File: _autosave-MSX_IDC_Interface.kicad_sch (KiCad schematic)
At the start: 27 parts, among them J1 DE1 GPIO, J2 Conn_01x03_Male, J3 Conn_01x03_Male, J4 Conn_01x03_Male, J5 Conn_01x03_Male, J6 Conn_01x03_Male, J7 Conn_01x03_Male, Q1 2N2222, Q2 2N2222, U1 74LVC245A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

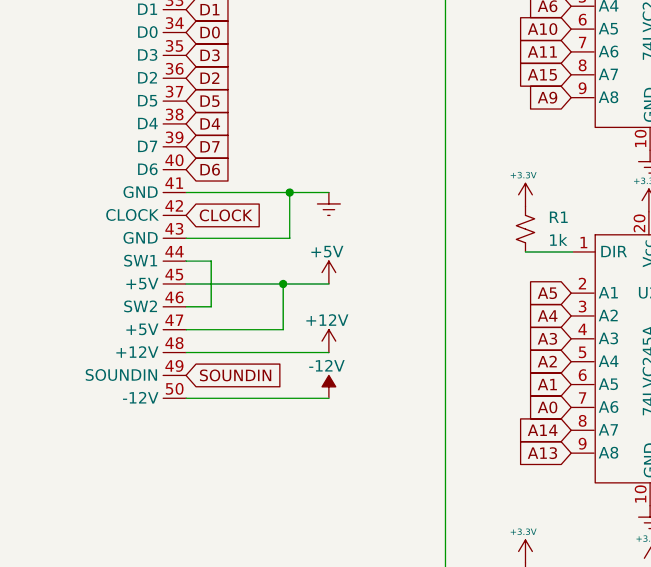
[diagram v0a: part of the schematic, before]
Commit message: Finished routing. Rules chekc not done yet
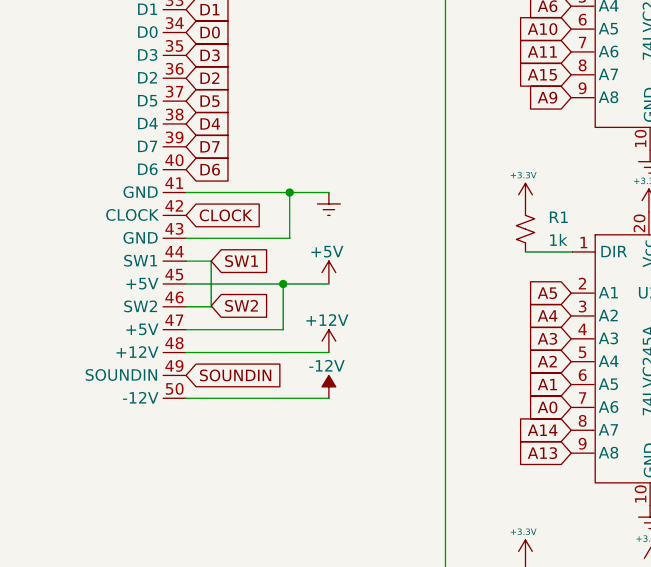
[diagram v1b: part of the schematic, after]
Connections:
- net SW1: now reaches CONN1.44 (SW1), CONN1.46 (SW2)
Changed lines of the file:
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@@
+    )
+  )
+  (global_label "SW1" (shape input) (at 35.1862 178.308 0) (fields_autoplaced)
+    (effects (font (size 1.27 1.27)) (justify left))
+    (property "Intersheet References" "${INTERSHEET_REFS}" (id 0) (at 41.4698 178.2286 0)
+      (effects (font (size 1.27 1.27)) (justify left) hide)
     )
   )
@@
     (property "Intersheet References" "${INTERSHEET_REFS}" (id 0) (at 65.6952 65.3574 0)
       (effects (font (size 1.27 1.27)) (justify right) hide)
+    )
+  )
+  (global_label "SW2" (shape input) (at 35.1862 183.2825 0) (fields_autoplaced)
+    (effects (font (size 1.27 1.27)) (justify left))
+    (property "Intersheet References" "${INTERSHEET_REFS}" (id 0) (at 41.4698 183.2031 0)
+      (effects (font (size 1.27 1.27)) (justify left) hide)
     )
   )
@@
   (symbol (lib_id "power:GNDREF") (at 109.5184 219.583 0) (unit 1)
     (in_bom yes) (on_board yes) (fields_autoplaced)
-    (property "Reference" "#PWR?" (id 0) (at 109.5184 225.933 0)
+    (property "Reference" "#PWR0104" (id 0) (at 109.5184 225.933 0)
       (effects (font (size 1.27 1.27)) hide)
     )
@@
   (symbol (lib_id "power:GNDREF") (at 108.204 100.203 0) (unit 1)
     (in_bom yes) (on_board yes) (fields_autoplaced)
-    (property "Reference" "#PWR?" (id 0) (at 108.204 106.553 0)
+    (property "Reference" "#PWR0105" (id 0) (at 108.204 106.553 0)
       (effects (font (size 1.27 1.27)) hide)
     )
@@
   (symbol (lib_id "power:GNDREF") (at 108.204 60.706 0) (unit 1)
     (in_bom yes) (on_board yes) (fields_autoplaced)
-    (property "Reference" "#PWR?" (id 0) (at 108.204 67.056 0)
+    (property "Reference" "#PWR0106" (id 0) (at 108.204 67.056 0)
       (effects (font (size 1.27 1.27)) hide)
     )
@@
   (symbol (lib_id "power:GNDREF") (at 108.847 140.2388 0) (unit 1)
     (in_bom yes) (on_board yes) (fields_autoplaced)
-    (property "Reference" "#PWR?" (id 0) (at 108.847 146.5888 0)
+    (property "Reference" "#PWR0102" (id 0) (at 108.847 146.5888 0)
       (effects (font (size 1.27 1.27)) hide)
     )
@@
   (symbol (lib_id "power:GNDREF") (at 109.3105 179.832 0) (unit 1)
     (in_bom yes) (on_board yes) (fields_autoplaced)
-    (property "Reference" "#PWR?" (id 0) (at 109.3105 186.182 0)
+    (property "Reference" "#PWR0103" (id 0) (at 109.3105 186.182 0)
       (effects (font (size 1.27 1.27)) hide)
     )
@@
       (reference "#PWR0101") (unit 1) (value "GNDREF") (footprint "")
     )
+    (path "/a7f26d93-3fc6-4423-a4ed-f0b3b4593cdf"
+      (reference "#PWR0102") (unit 1) (value "GNDREF") (footprint "")
+    )
+    (path "/c5bbbada-72d1-4e17-b89e-b50fc48d510b"
+      (reference "#PWR0103") (unit 1) (value "GNDREF") (footprint "")
+    )
     (path "/1b971c98-c17e-40e4-bf31-2e4c8421e525"
-      (reference "#PWR?") (unit 1) (value "GNDREF") (footprint "")
+      (reference "#PWR0104") (unit 1) (value "GNDREF") (footprint "")
     )
     (path "/2723d1e6-27f9-43a4-b74d-6d99578b38b4"
-      (reference "#PWR?") (unit 1) (value "GNDREF") (footprint "")
+      (reference "#PWR0105") (unit 1) (value "GNDREF") (footprint "")
     )
     (path "/326dad68-18c6-41b2-abe2-63b86d607d3f"
-      (reference "#PWR?") (unit 1) (value "GNDREF") (footprint "")
-    )
-    (path "/a7f26d93-3fc6-4423-a4ed-f0b3b4593cdf"
-      (reference "#PWR?") (unit 1) (value "GNDREF") (footprint "")
-    )
-    (path "/c5bbbada-72d1-4e17-b89e-b50fc48d510b"
-      (reference "#PWR?") (unit 1) (value "GNDREF") (footprint "")
+      (reference "#PWR0106") (unit 1) (value "GNDREF") (footprint "")
     )
     (path "/d88b88a1-3a49-411f-ab35-844e3052fd45"
